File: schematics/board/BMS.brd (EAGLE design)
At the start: 68 x 22 mm, 11 parts

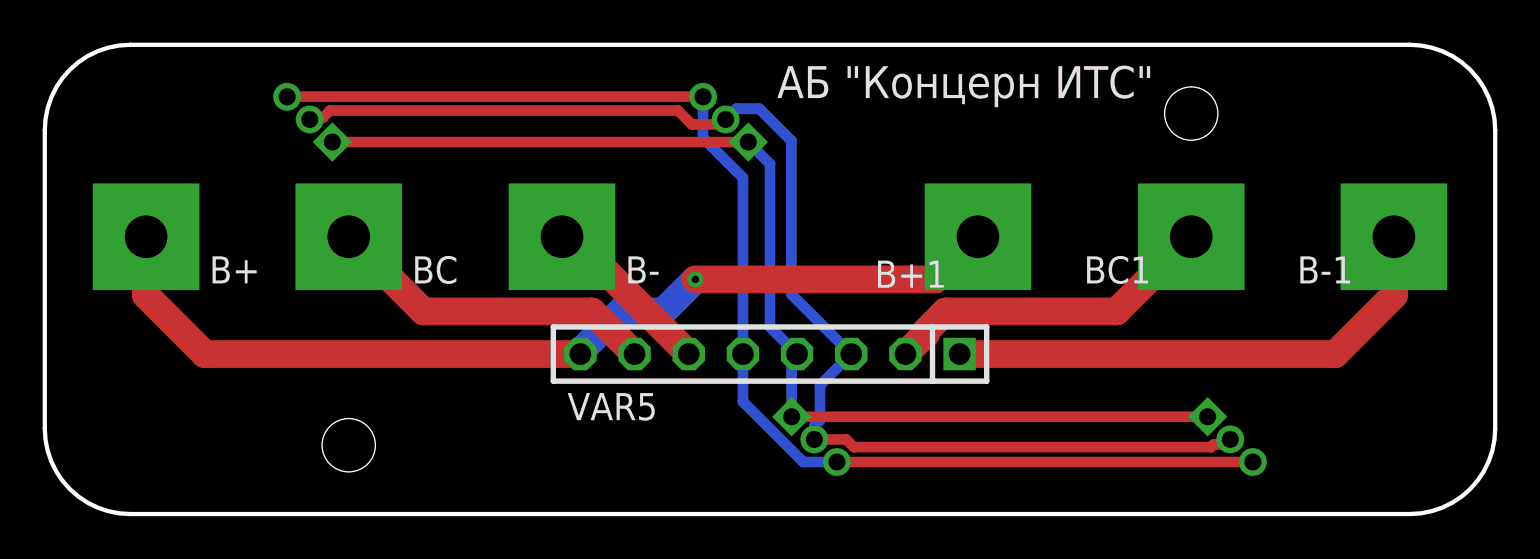
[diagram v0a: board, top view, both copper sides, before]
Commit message: Исправлены ошибки в плате АБ
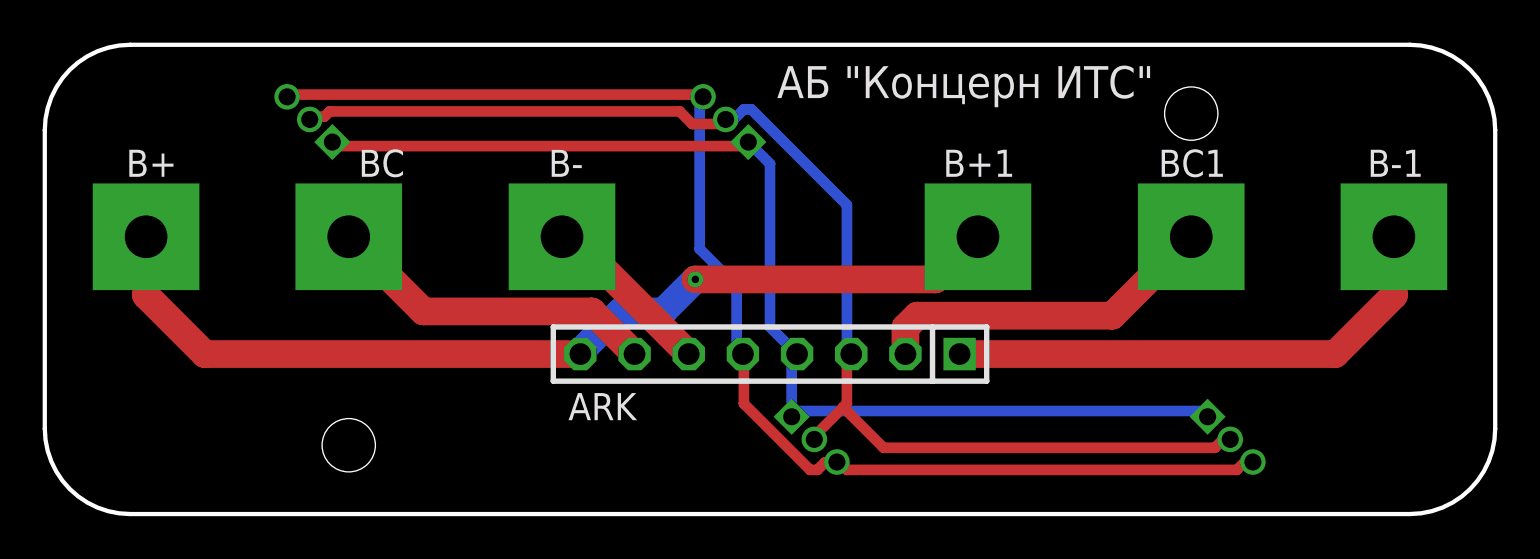
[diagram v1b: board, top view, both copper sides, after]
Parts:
- renumbered VAR5 to ARK
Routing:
- net 1W: track 59.6 -> 58.6 mm
- net VDD: track 59.6 -> 60.6 mm
- net N$206: track 15.7 -> 16.4 mm
- net N$1: track 52.9 -> 53.5 mm
